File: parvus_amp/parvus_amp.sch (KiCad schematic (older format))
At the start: 40 parts, among them J1 input, J2 output, J3 powersupply, U1 LM3886

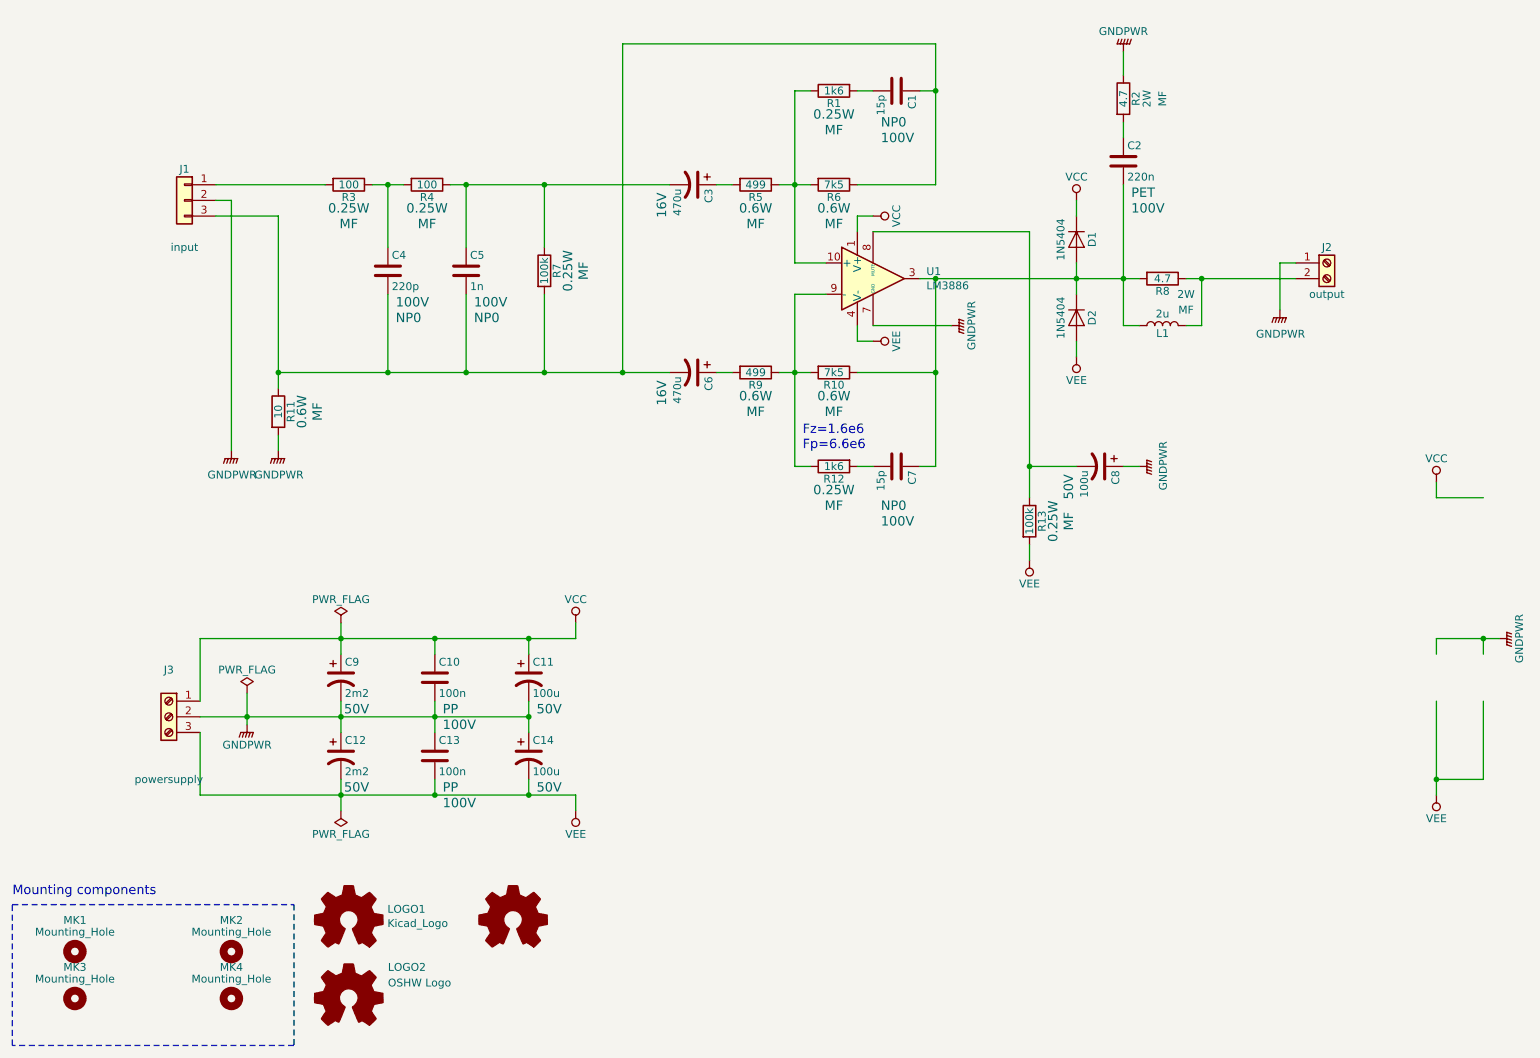
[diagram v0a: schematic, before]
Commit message: Added a bunch of documentation.
Signed-off-by: Nenad Radulovic <nenad.b.radulovic@gmail.com>
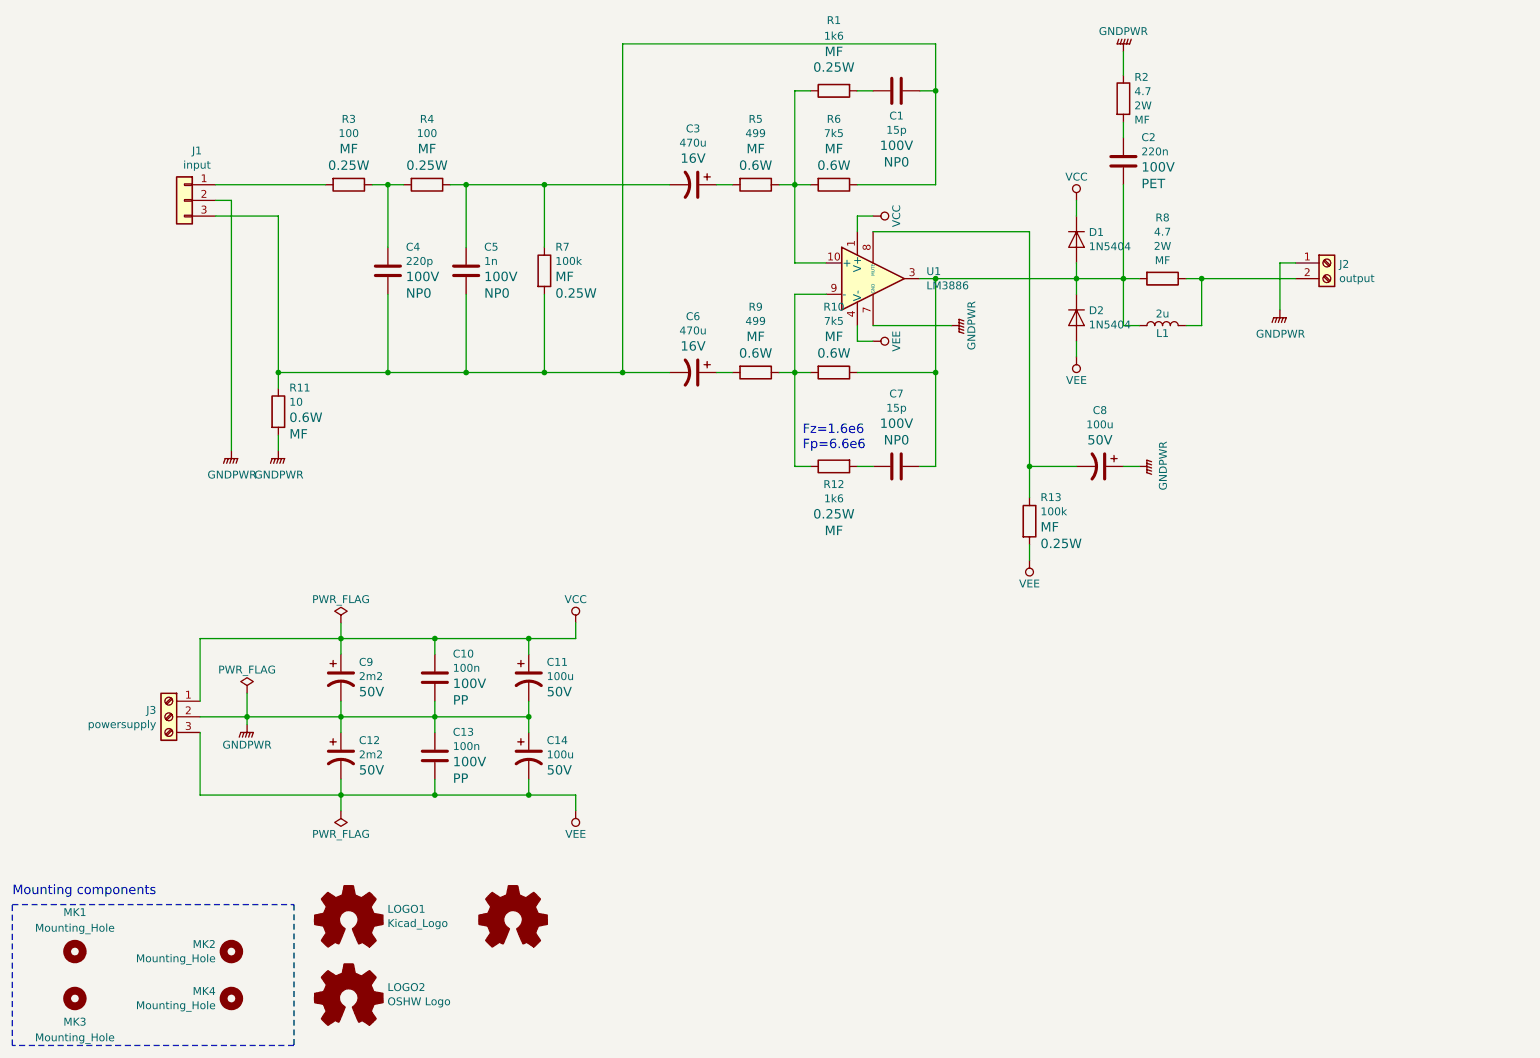
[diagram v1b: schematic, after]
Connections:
- wire segments 121 -> 111

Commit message: Updated schematic and README description
Signed-off-by: Nenad Radulovic <nenad.b.radulovic@gmail.com>
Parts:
- added C15: 100n, Capacitor_THT:C_Rect_L7.0mm_W3.5mm_P5.00mm, symbol Device:C
- added D1: BZX85C16, Diode_THT:D_DO-35_SOD27_P7.62mm_Horizontal, symbol Device:D_Zener
- added R14: 10, Resistor_THT:R_Axial_DIN0207_L6.3mm_D2.5mm_P10.16mm_Horizontal, symbol Device:R
- R11: renamed from R13; value 100k -> 7k5; Manufacturer TE Connectivity:LR0204F100K -> TE Connectivity:LR0204F7K5; Vendor Farnell:2329853 -> Farnell:2329974
- renumbered C9 to C1, C6 to C10, C1 to C11, C7 to C12, C8 to C13, C2 to C14, C12 to C2, C4 to C3, C10 to C4, C13 to C5, C5 to C6, C11 to C7, C14 to C8, C3 to C9, D1 to D2, D2 to D3, J3 to J1, J1 to J2, J2 to J3, MK3 to MK2, MK2 to MK3, R11 to R1, R12 to R10, R2 to R12, R8 to R13, R3 to R2, R4 to R3, R7 to R4, R9 to R6, R1 to R7, R6 to R8, R10 to R9
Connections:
- net GNDPWR: now also R14.1
- net at J3.2 (Pin_2), L1.2, R13.1: now also C15.2
- net at C13.2, R11.1: now also D1.2 (A); no longer U1.8 (MUTE)
- new net: D1.1 (K), U1.8 (MUTE)
- new net: C15.1, R14.2

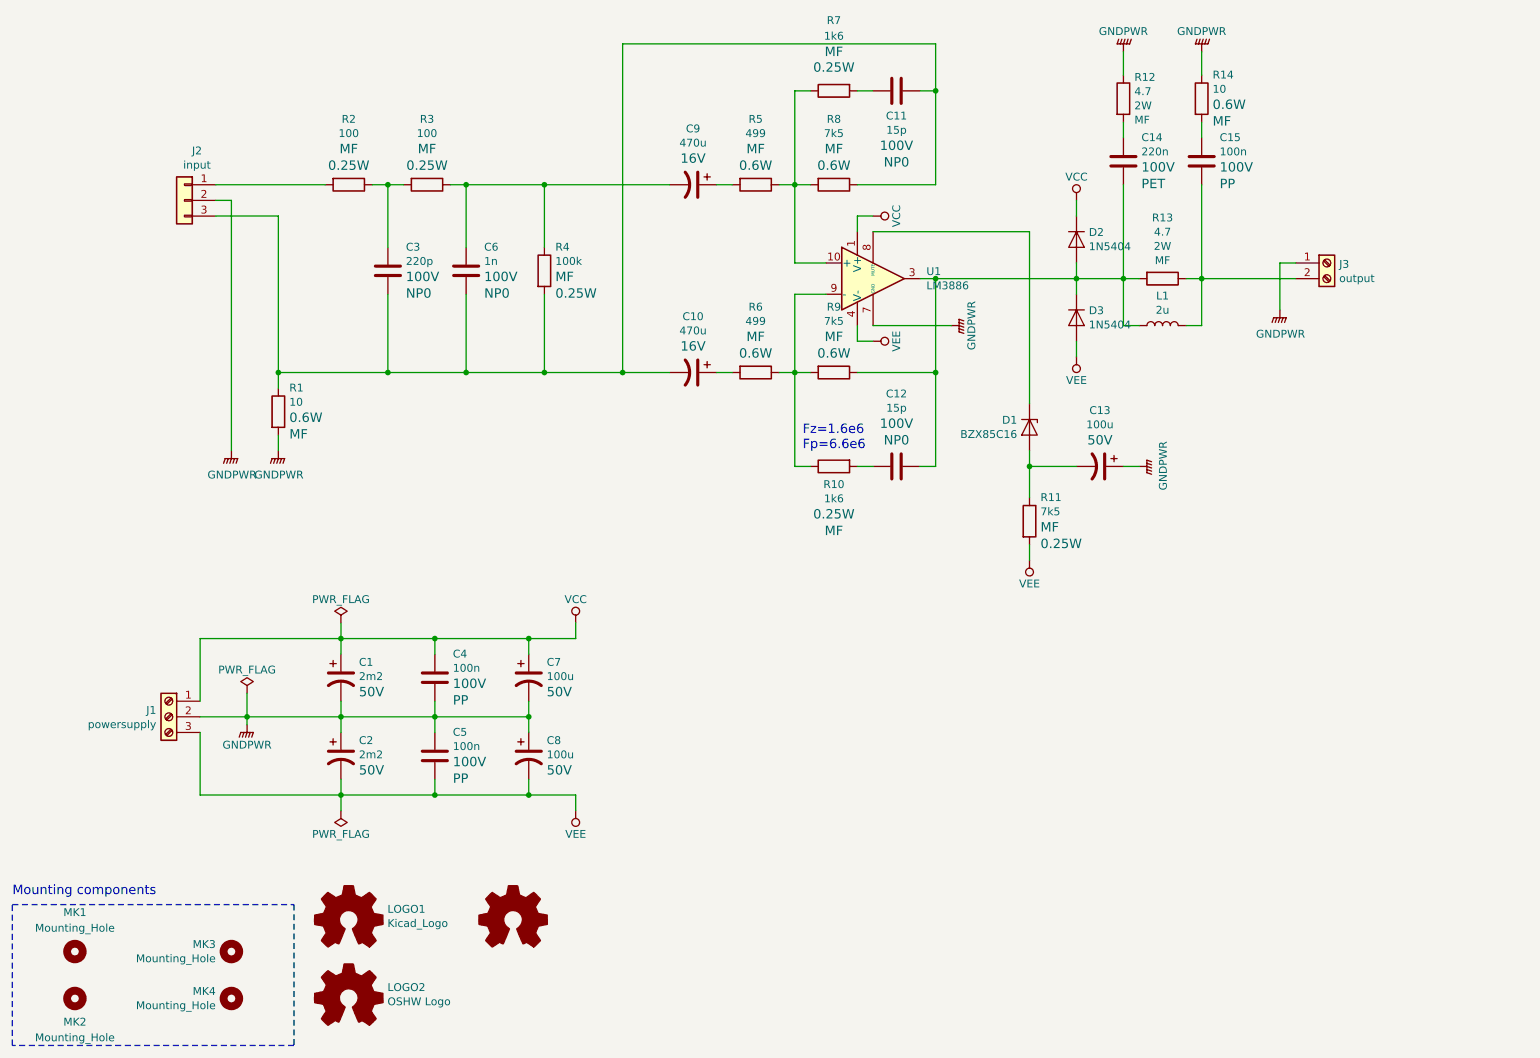
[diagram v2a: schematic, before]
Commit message: Using Phoenix MCV type of connectors
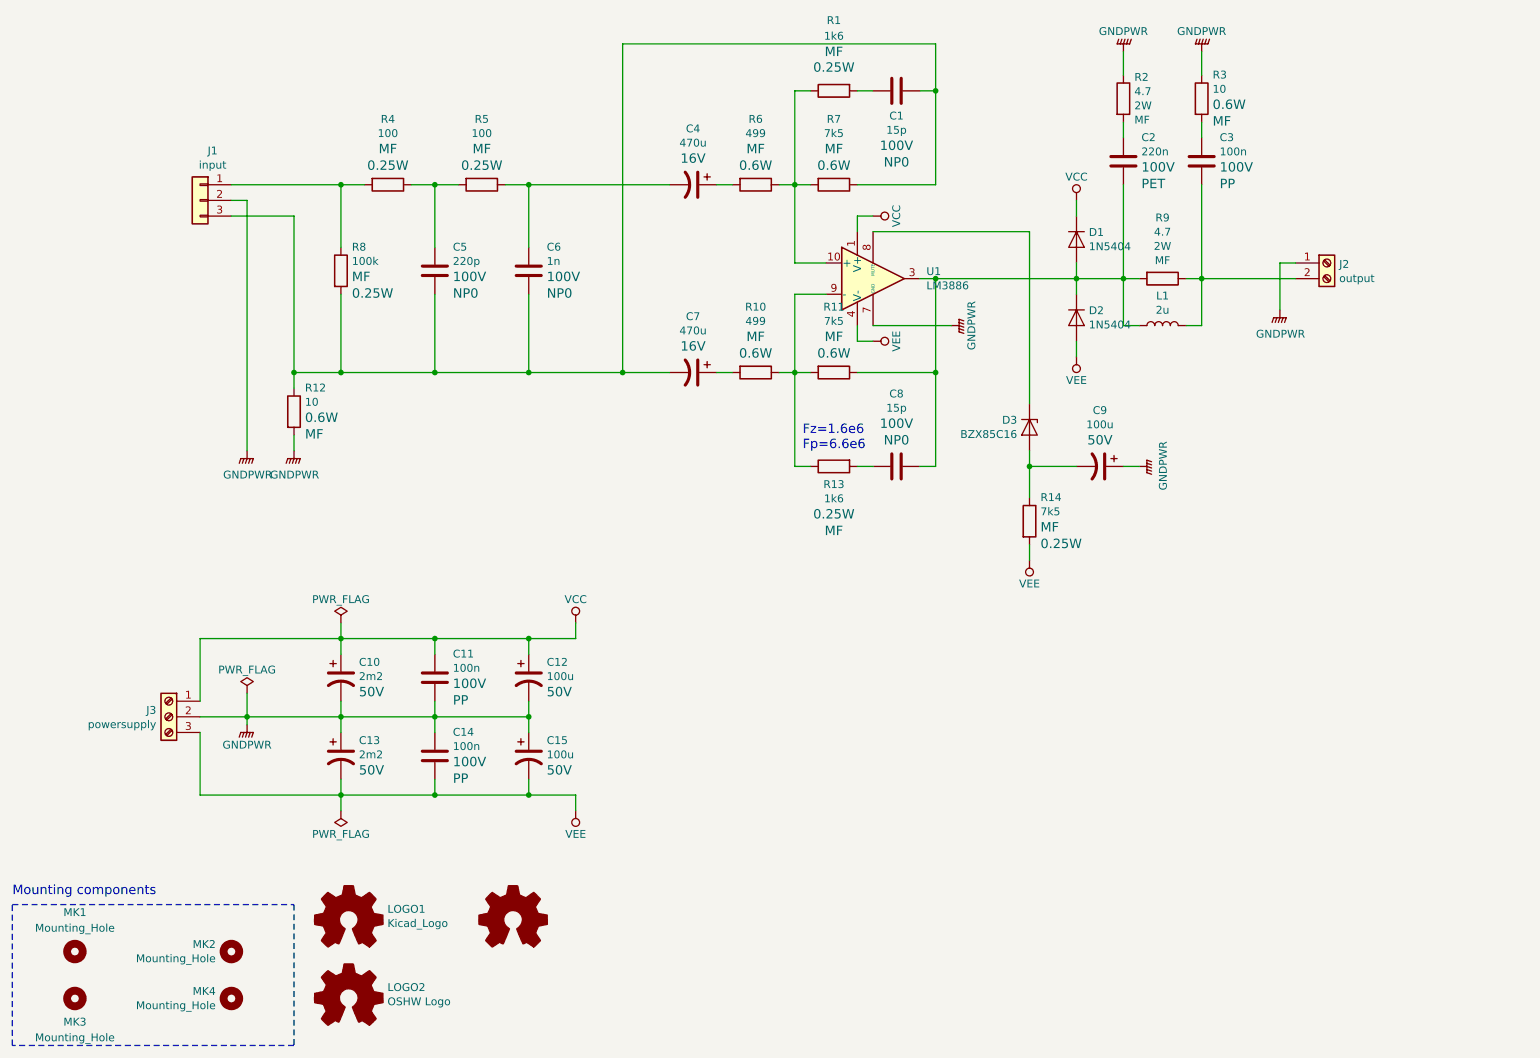
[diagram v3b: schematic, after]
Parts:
- J2: renamed from J3; footprint TerminalBlock_Phoenix:TerminalBlock_Phoenix_MKDS-3-2-5.08_1x02_P5.08mm_Horizontal -> Connector_Phoenix_MC:PhoenixContact_MCV_1,5_2-G-3.5_1x02_P3.50mm_Vertical
- J3: renamed from J1; footprint TerminalBlock_Phoenix:TerminalBlock_Phoenix_MKDS-3-3-5.08_1x03_P5.08mm_Horizontal -> Connector_Phoenix_MC:PhoenixContact_MCV_1,5_3-G-3.5_1x03_P3.50mm_Vertical
- renumbered C11 to C1, C1 to C10, C4 to C11, C7 to C12, C2 to C13, C5 to C14, C8 to C15, C14 to C2, C15 to C3, C9 to C4, C3 to C5, C10 to C7, C12 to C8, C13 to C9, D2 to D1, D3 to D2, D1 to D3, J2 to J1, MK3 to MK2, MK2 to MK3, R7 to R1, R6 to R10, R9 to R11, R1 to R12, R10 to R13, R11 to R14, R12 to R2, R14 to R3, R2 to R4, R3 to R5, R5 to R6, R8 to R7, R4 to R8, R13 to R9
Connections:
- net at C4.2, C6.1, R5.1: no longer R8.1
- net at J1.1 (Pin_1), R4.2: now also R8.1
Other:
- moved on the sheet: C5, C6, J1, R12, R4, R5, R8

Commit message: Finished the amp board.
Signed-off-by: Nenad Radulovic <nenad.b.radulovic@gmail.com>
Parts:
- removed C1: 15p, Capacitor_THT:C_Disc_D3.8mm_W2.6mm_P2.50mm, symbol Device:C
- removed C4: 470u, Capacitor_THT:CP_Radial_D8.0mm_P3.50mm, symbol Device:CP1
- removed C5: 220p, Capacitor_THT:C_Disc_D4.3mm_W1.9mm_P5.00mm, symbol Device:C
- removed R1: 1k6, Resistor_THT:R_Axial_DIN0207_L6.3mm_D2.5mm_P7.62mm_Horizontal, symbol Device:R
- removed R5: 100, Resistor_THT:R_Axial_DIN0207_L6.3mm_D2.5mm_P7.62mm_Horizontal, symbol Device:R
- removed R6: 499, Resistor_THT:R_Axial_DIN0207_L6.3mm_D2.5mm_P10.16mm_Horizontal, symbol Device:R
- added C3: 100u, Capacitor_THT:CP_Radial_D8.0mm_P3.50mm, symbol Device:CP1
- added C6: 2n2, Capacitor_THT:C_Disc_D5.1mm_W3.2mm_P5.00mm, symbol Device:C
- added R3: 100, Resistor_THT:R_Axial_DIN0207_L6.3mm_D2.5mm_P10.16mm_Horizontal, symbol Device:R
- C1: renamed from C10; Manufacturer Rubycon:50YXJ2200M16X35.5 -> (none); ManufacturerA (none) -> Rybicon:50YXJ2200M16X35.5; SupplierA1 (none) -> Farnell:2346272; Vendor Farnell:2346272 -> (none)
- C10: renamed from C9; Manufacturer Rybicon:35ML100MEFC8X7.5 -> (none); ManufacturerA (none) -> Rybicon:50YXJ100MT78X11.5; SupplierA1 (none) -> Farnell:2346269; Vendor Farnell:8126550 -> (none)
- C11: renamed from C2; Manufacturer WIMA:MKS2D032201C00KSSD -> (none); ManufacturerA (none) -> WIMA:MKS2D032201C00KSSD; SupplierA1 (none) -> Farnell:1890146; SupplierA2 (none) -> Mouser: 505-MKS2.22/100/10; SupplierA3 (none) -> Digikey: 1928-1659-ND; Vendor Farnell:1890146 -> (none)
- C12: renamed from C3; Manufacturer WIMA:MKP2D031001F00KSSD -> (none); ManufacturerA (none) -> WIMA:MKP2D031001F00KSSD; SupplierA1 (none) -> Farnell:1890265; SupplierA2 (none) -> Mouser: 505-MKP2.1/100/10; Vendor Farnell:1890265 -> (none)
- C2: renamed from C13; Manufacturer Rubycon:50YXJ2200M16X35.5 -> (none); ManufacturerA (none) -> Rybicon:50YXJ2200M16X35.5; SupplierA1 (none) -> Farnell:2346272; Vendor Farnell:2346272 -> (none)
- C4: renamed from C12; Manufacturer Rybicon:50YXJ100MT78X11.5 -> (none); ManufacturerA (none) -> Rybicon:50YXJ100MT78X11.5; SupplierA1 (none) -> Farnell:2346269; Vendor Farnell:2346269 -> (none)
- C5: renamed from C15; Manufacturer Rybicon:50YXJ100MT78X11.5 -> (none); ManufacturerA (none) -> Rybicon:50YXJ100MT78X11.5; SupplierA1 (none) -> Farnell:2346269; Vendor Farnell:2346269 -> (none)
- C7: renamed from C6; value 1n -> 2n2; footprint Capacitor_THT:C_Disc_D4.3mm_W1.9mm_P5.00mm -> Capacitor_THT:C_Disc_D5.1mm_W3.2mm_P5.00mm; Manufacturer AVX:SR211A102KAR -> (none); ManufacturerA (none) -> AVX: SR211A222JAR; SupplierA1 (none) -> Farnell: 1100515; SupplierA2 (none) -> Mouser: 581-SR211A222JAR; Vendor Farnell:1100513 -> (none)
- C8: renamed from C11; Manufacturer WIMA:MKP2D031001F00KSSD -> (none); ManufacturerA (none) -> WIMA:MKP2D031001F00KSSD; SupplierA1 (none) -> Farnell:1890265; SupplierA2 (none) -> Mouser: 505-MKP2.1/100/10; Vendor Farnell:1890265 -> (none)
- C9: renamed from C14; Manufacturer WIMA:MKP2D031001F00KSSD -> (none); ManufacturerA (none) -> WIMA:MKP2D031001F00KSSD; SupplierA1 (none) -> Farnell:1890265; SupplierA2 (none) -> Mouser: 505-MKP2.1/100/10; Vendor Farnell:1890265 -> (none)
- Cf1: renamed from C8; value 15p -> 68p; Manufacturer AVX:SR151A150JAR -> (none); ManufacturerA (none) -> AVX: SR151A680JAR; SupplierA1 (none) -> Farnell: 2332952; SupplierA2 (none) -> Mouser: 581-SR151A680JAR; Vendor Farnel:1100498 -> (none)
- Ci1: renamed from C7; value 470u -> 2m2; footprint Capacitor_THT:CP_Radial_D8.0mm_P3.50mm -> Capacitor_THT:CP_Radial_D10.0mm_P3.50mm; Manufacturer Rybicon:16YXJ470M8X11.5 -> (none); ManufacturerA (none) -> Rybicon:16YXJ470M8X11.5; SupplierA1 (none) -> Farnell:114461; Vendor Farnell:1144610 -> (none)
- D1: renamed from D3; footprint Diode_THT:D_DO-35_SOD27_P7.62mm_Horizontal -> Diode_THT:D_DO-35_SOD27_P10.16mm_Horizontal; Manufacturer ON Semiconducter:BZX79C15 -> (none); ManufacturerA (none) -> ON Semiconducter:BZX79C15; SupplierA1 (none) -> Farnell: 146759; Vendor Farnell: 1467595 -> (none)
- D2: renamed from D1; Manufacturer ON Semiconductor:1N5404RL -> (none); ManufacturerA (none) -> ON Semiconductor:1N5404RL; SupplierA1 (none) -> Farnell:955614; Vendor Farnell:9556141 -> (none)
- D3: renamed from D2; Manufacturer ON Semiconductor:1N5404RL -> (none); ManufacturerA (none) -> ON Semiconductor:1N5404RL; SupplierA1 (none) -> Farnell:955614; Vendor Farnell:9556141 -> (none)
- J1: renamed from J3; footprint Connector_Phoenix_MC:PhoenixContact_MCV_1,5_3-G-3.5_1x03_P3.50mm_Vertical -> Connector_Phoenix_MC:PhoenixContact_MCV_1,5_4-G-3.5_1x04_P3.50mm_Vertical; symbol Connector:Screw_Terminal_01x03 -> Connector:Screw_Terminal_01x04; Manufacturer Phoenix:MKDSN2,5/3-5.08 -> (none); ManufacturerA (none) -> Phoenix: MKDSN2,5/4-5.08 (1888700); SupplierA1 (none) -> Farnell: 1792768; Vendor Farnell:1792767 -> (none)
- J2: renamed from J1; Manufacturer Phoenix:MKDS1/3-3,5 -> (none); ManufacturerA (none) -> Phoenix:MKDS1/3-3,5; SupplierA1 (none) -> Farnell:247858; Vendor Farnell:2478587 -> (none)
- J3: renamed from J2; Manufacturer Phoenix:MKDSN2,5/2-5.08 -> (none); ManufacturerA (none) -> Phoenix:MKDSN2,5/2-5.08; SupplierA1 (none) -> Farnell:179276; Vendor Farnell:1792766 -> (none)
- L1: footprint Inductor_THT:L_Axial_L12.0mm_D5.0mm_P15.24mm_Horizontal_Fastron_MISC -> Inductor_THT:L_Axial_L9.5mm_D4.0mm_P12.70mm_Horizontal_Fastron_SMCC
- R1: renamed from R12; Manufacturer TE Connectivity:LR1F10R -> (none); ManufacturerA (none) -> Vishay: MRS25000C1009FRP00; SupplierA1 (none) -> Farnell: 1771968; SupplierA2 (none) -> Mouser: 594-MRS25000C1000FRP; Vendor Farnell:2329993 -> (none)
- R2: renamed from R8; footprint Resistor_THT:R_Axial_DIN0207_L6.3mm_D2.5mm_P7.62mm_Horizontal -> Resistor_THT:R_Axial_DIN0207_L6.3mm_D2.5mm_P10.16mm_Horizontal; Manufacturer TE Connectivity:LR0204F100K -> (none); ManufacturerA (none) -> Vishay: MRS25000C1003FRP00; Power 0.25W -> 0.6W; SupplierA1 (none) -> Farnell: 1771967; SupplierA2 (none) -> Mouser: 594-MRS25000C1003FRP; Vendor Farnell:2329853 -> (none)
- R4: footprint Resistor_THT:R_Axial_DIN0207_L6.3mm_D2.5mm_P7.62mm_Horizontal -> Resistor_THT:R_Axial_DIN0207_L6.3mm_D2.5mm_P10.16mm_Horizontal; Manufacturer TE Connectivity:LR0204F100R -> (none); ManufacturerA (none) -> Vishay: MRS25000C1000FRP00; Power 0.25W -> 0.6W; SupplierA1 (none) -> Farnell: 1771963; SupplierA2 (none) -> Mouser: 594-MRS25000C1000FRP; Vendor Farnell:2329854 -> (none)
- R5: renamed from R7; value 7k5 -> 1k5; Manufacturer TE Connectivity:LR1F7K5 -> (none); ManufacturerA (none) -> Vishay: MRS25000C1501FRP00; SupplierA1 (none) -> Farnell: 1771971; SupplierA2 (none) -> Mouser: 594-MRS25000C1501FRP; Vendor Farnell:2330223 -> (none)
- R6: renamed from R14; footprint Resistor_THT:R_Axial_DIN0207_L6.3mm_D2.5mm_P7.62mm_Horizontal -> Resistor_THT:R_Axial_DIN0207_L6.3mm_D2.5mm_P10.16mm_Horizontal; Manufacturer TE Connectivity:LR0204F7K5 -> (none); ManufacturerA (none) -> Vishay: MRS25000C7501FCT00; Power 0.25W -> 0.6W; SupplierA1 (none) -> Farnell: 9470115; SupplierA2 (none) -> Mouser: 594-MRS25000C7501FRP; Vendor Farnell:2329974 -> (none)
- R7: renamed from R2; footprint Resistor_THT:R_Axial_DIN0411_L9.9mm_D3.6mm_P15.24mm_Horizontal -> Resistor_THT:R_Axial_DIN0411_L9.9mm_D3.6mm_P12.70mm_Horizontal; Manufacturer Vishay:PR02000204708JA100 -> (none); ManufacturerA (none) -> Vishay: PR02000204708JR500; SupplierA1 (none) -> Farnell: 1775179; SupplierA2 (none) -> Mouser: 594-5083NW4R700J; Vendor Farnell:2614544 -> (none)
- R8: renamed from R9; footprint Resistor_THT:R_Axial_DIN0411_L9.9mm_D3.6mm_P15.24mm_Horizontal -> Resistor_THT:R_Axial_DIN0411_L9.9mm_D3.6mm_P12.70mm_Horizontal; Manufacturer Vishay:PR02000204708JA100 -> (none); ManufacturerA (none) -> Vishay: PR02000204708JR500; SupplierA1 (none) -> Farnell: 1775179; SupplierA2 (none) -> Mouser: 594-5083NW4R700J; Vendor Farnell:2614544 -> (none)
- R9: renamed from R3; Manufacturer TE Connectivity:LR1F10R -> (none); ManufacturerA (none) -> Vishay: MRS25000C1009FRP00; SupplierA1 (none) -> Farnell: 1771968; SupplierA2 (none) -> Mouser: 594-MRS25000C1000FRP; Vendor Farnell:2329993 -> (none)
- Rf1: renamed from R11; value 7k5 -> 1k5; footprint Resistor_THT:R_Axial_DIN0207_L6.3mm_D2.5mm_P10.16mm_Horizontal -> Resistor_THT:R_Axial_DIN0411_L9.9mm_D3.6mm_P12.70mm_Horizontal; Manufacturer TE Connectivity:LR1F7K5 -> (none); ManufacturerA (none) -> Vishay: PR02000201501JR500; Power 0.6W -> 2W; SupplierA1 (none) -> Farnell: 1772519; SupplierA2 (none) -> Mouser: 594-5083NW1K500J; Vendor Farnell:2330223 -> (none)
- Rf2: renamed from R13; value 1k6 -> 430; footprint Resistor_THT:R_Axial_DIN0207_L6.3mm_D2.5mm_P7.62mm_Horizontal -> Resistor_THT:R_Axial_DIN0207_L6.3mm_D2.5mm_P10.16mm_Horizontal; Manufacturer TE Connectivity:LR0204F1K6 -> (none); ManufacturerA (none) -> Vishay: MRS25000C4300FCT00; Power 0.25W -> 0.6W; SupplierA1 (none) -> Farnell: 9468269; Vendor Farnell:2329892 -> (none)
- Ri1: renamed from R10; value 499 -> 100; Manufacturer TE Connectivity:LR1F499R -> (none); ManufacturerA (none) -> Vishay: MRS25000C1000FRP00; SupplierA1 (none) -> Farnell: 1771963; SupplierA2 (none) -> Mouser: 594-MRS25000C1000FRP; Vendor Farnell:2330163 -> (none)
- renumbered MK3 to MK2, MK2 to MK3
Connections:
- net GNDPWR: now also C11.1, C12.1, J1.3 (Pin_3), J3.2 (Pin_2); no longer J1.2 (Pin_2), J3.1 (Pin_1), R7.1, R9.1
- net VCC: now also J1.4 (Pin_4); no longer J1.1 (Pin_1)
- net VEE: now also J1.2 (Pin_2); no longer J1.3 (Pin_3), R6.2
- net at L1.2, R8.1: now also J3.1 (Pin_1), R9.2; no longer C12.2, J3.2 (Pin_2)
- net out: now reaches D2.2 (A), D3.1 (K), L1.1, R8.2, Rf1.1, U1.3
- net out: now also R7.2, Rf2.2; no longer C11.2, Cf1.1
- net at C7.1: now also R4.1, R5.2, U1.10 (+)
- net at Rf1.2, Ri1.1, U1.9 (-): now also Cf1.2; no longer Rf2.1
- net sgnd: now reaches C7.2, Ci1.2, J2.3 (Pin_3), R1.1, R2.2, R5.1
- net sgnd: now also C6.2
- net at J2.1 (Pin_1), R2.1: now also C3.2; no longer R4.2
- new net: C11.2, R7.1
- new net: Cf1.1, Rf2.1
- new net: J1.1 (Pin_1), R6.2
- new net: C12.2, R9.1
- new net: C6.1, R3.1, R4.2
- new net: C3.1, R3.2
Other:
- note added: "Fz=1/(2*pi*Rf1*Cf)\nFp=1/(2*pi*Rf2*Cf)\n"
- moved on the sheet: C1, C11, C12, C2, C4, C5, C8, C9, Cf1, R5, R7, R9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
